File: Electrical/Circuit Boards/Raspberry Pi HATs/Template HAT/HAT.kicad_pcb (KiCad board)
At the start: 2 copper layers, 65 x 30 mm, 19 parts, among them J1 CONN_02X01, J2 CONN_02X20, Q1 DMMT5401, Q2 DMG2305UX, U1 CAT24C32WI-GT3

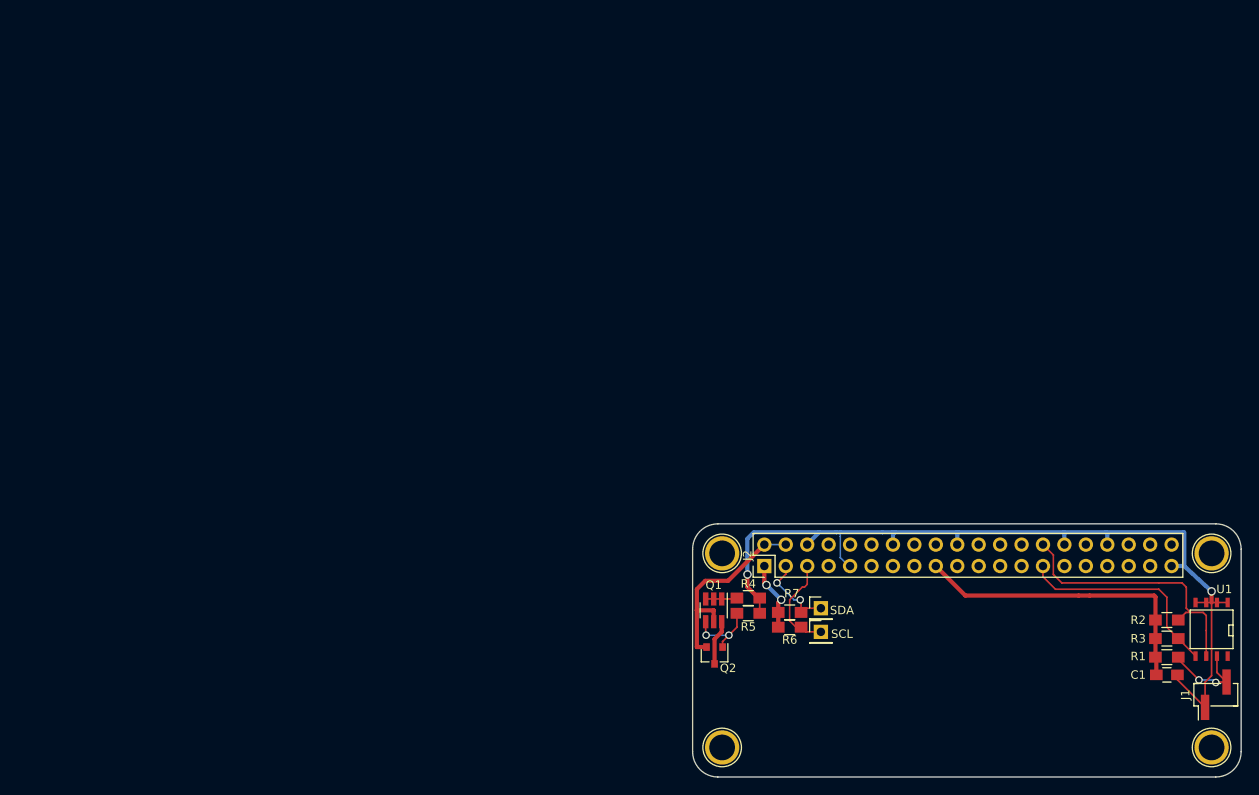
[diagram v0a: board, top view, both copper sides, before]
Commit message: Added an 8-channel ADC HAT (10 kHz chip)
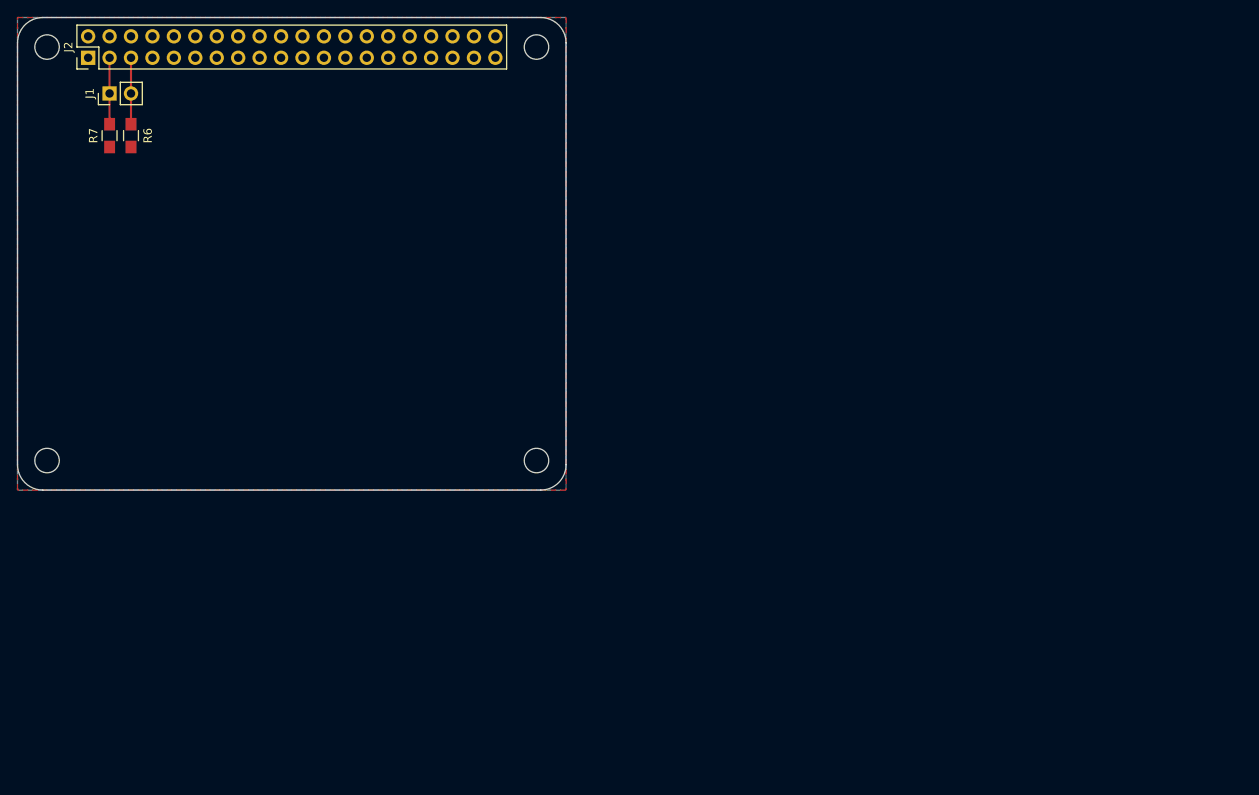
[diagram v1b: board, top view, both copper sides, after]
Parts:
- removed C1: 100n, Capacitors_SMD:C_0805_HandSoldering
- removed Q1: DMMT5401, TO_SOT_Packages_SMD:SOT-23-6_Handsoldering
- removed Q2: DMG2305UX, modules:SOT-23
- removed R1: 1K, Resistors_SMD:R_0805_HandSoldering
- removed R2, R3: 3.9K, Resistors_SMD:R_0805_HandSoldering
- removed R4: 10K, Resistors_SMD:R_0805_HandSoldering
- removed R5: 47K, Resistors_SMD:R_0805_HandSoldering
- removed REF** (x4): 1pin, Connectors:1pin
- removed SCL, SDA: TEST, Pin_Headers:Pin_Header_Straight_1x01_Pitch2.54mm
- removed U1: CAT24C32WI-GT3, SMD_Packages:SOIC-8-N
- J1: value CONN_02X01 -> CONN_01X02; footprint Pin_Headers:Pin_Header_Straight_1x02_Pitch2.54mm_SMD_Pin1Left -> Pin_Headers:Pin_Header_Straight_1x02_Pitch2.54mm
- moved J1 149.2 mm to (110.9, 84.0)
- moved J2 100.2 mm to (108.4, 79.8)
- moved R7 98.4 mm to (110.9, 89.0), turned to 90 degrees
- moved R6 97.4 mm to (113.5, 89.0), turned to 90 degrees
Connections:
- J1 pad 1: GND -> /SDA
- J1 pad 2: Net-(J1-Pad2) -> /SCL
- J2 pad 2: /Pi Connector/+5V_Pi -> +5V
- J2 pad 4: /Pi Connector/+5V_Pi -> +5V
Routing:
- net GND: track 108.5 -> 0.00 mm, vias 2 -> 0
- net +3V3: track 45.1 -> 0.00 mm, vias 2 -> 0
- net /Pi Connector/ID_SC: track 32.3 -> 0.00 mm
- net /Pi Connector/ID_SD: track 25.3 -> 0.00 mm
- net /Pi Connector/+5V_Pi: track 24.1 -> 0.00 mm
- net Net-(J1-Pad2): track 10.7 -> 0.00 mm, vias 2 -> 0
- net Net-(Q1-Pad4): track 9.02 -> 0.00 mm, vias 2 -> 0
- net +5V: track 5.35 -> 0.00 mm
- net Net-(Q1-Pad1): track 3.88 -> 0.00 mm
- net /SCL: track 11.7 -> 7.88 mm
- net /SDA: track 10.8 -> 7.88 mm, vias 2 -> 0
- added copper zone on F.Cu, net +3V3
- added copper zone on B.Cu, net GND
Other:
- board size 65 x 30 mm -> 65 x 56 mm
- net class Default: trace_width 0.2 -> 0.25; via_dia 0.9 -> 0.6; via_drill 0.6 -> 0.4
- net class Power removed
- rule pad_to_mask_clearance: 0 -> 0.2
- rule trace_min: 0.1524 -> 0.2
- rule via_min_drill: 0.5 -> 0.3
- rule via_min_size: 0.8 -> 0.4
